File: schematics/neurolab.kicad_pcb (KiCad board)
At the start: 2 copper layers, 127 x 53.6 mm, 167 parts, among them J1 GS3, J10 GS3, J12 GS3, J13 GS3, J14 GS3, J15 GS3, J16 Channel, J17 External, J18 USB_OTG, J19 GS3, J2 GS3, J20 GS2, J21 GS2, J22 GS2, J23 GS2, J24 GS2, J25 GS2, J26 ICSP Port, J27 GS2, J28 GS2, J3 GS3, J32 Bluetooth, J33 Reset Select, J34 GS2, J4 GS2, J5 GS2, J6 GS3, J7 GS3, J8 PowerOut, J9 GS3, Q1 2N7002, U1 ADP1720ARMZ-5, U10 OPA2111KP, U11 AD8422ARMZ, U12 OP4117, U13 OPA2111KP, U14 AD8422ARMZ, U15 OP4117, U16 AD7173, U17 ADR445BR, U18 Arduino, U2 ADP1720ARMZ-3.3, U3 AD8475, U4 AD8475, U5 MAX7480ESA+, U6 MAX7480ESA+, U7 MAX7480ESA+, U8 MAX7480ESA+, U9 TLC555CD, Y1 FA-20H

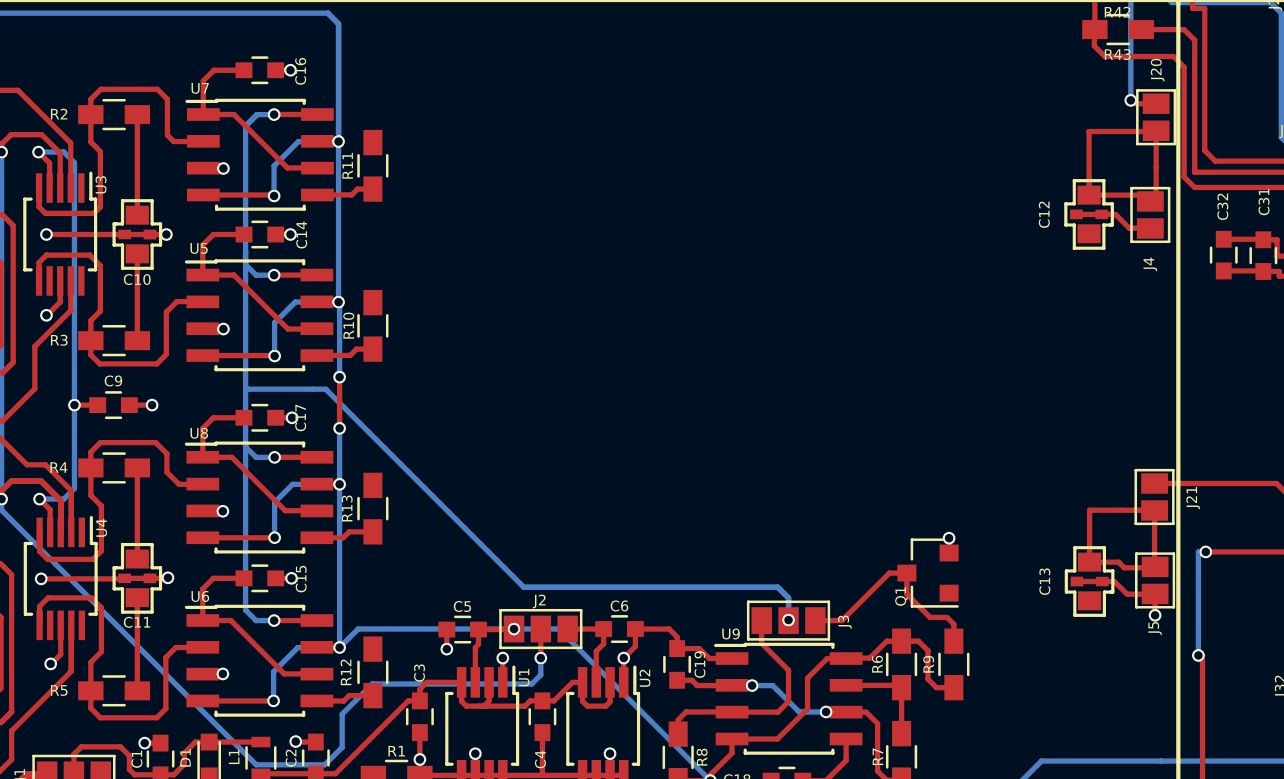
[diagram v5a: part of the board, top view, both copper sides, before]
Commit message: optimize: route parts
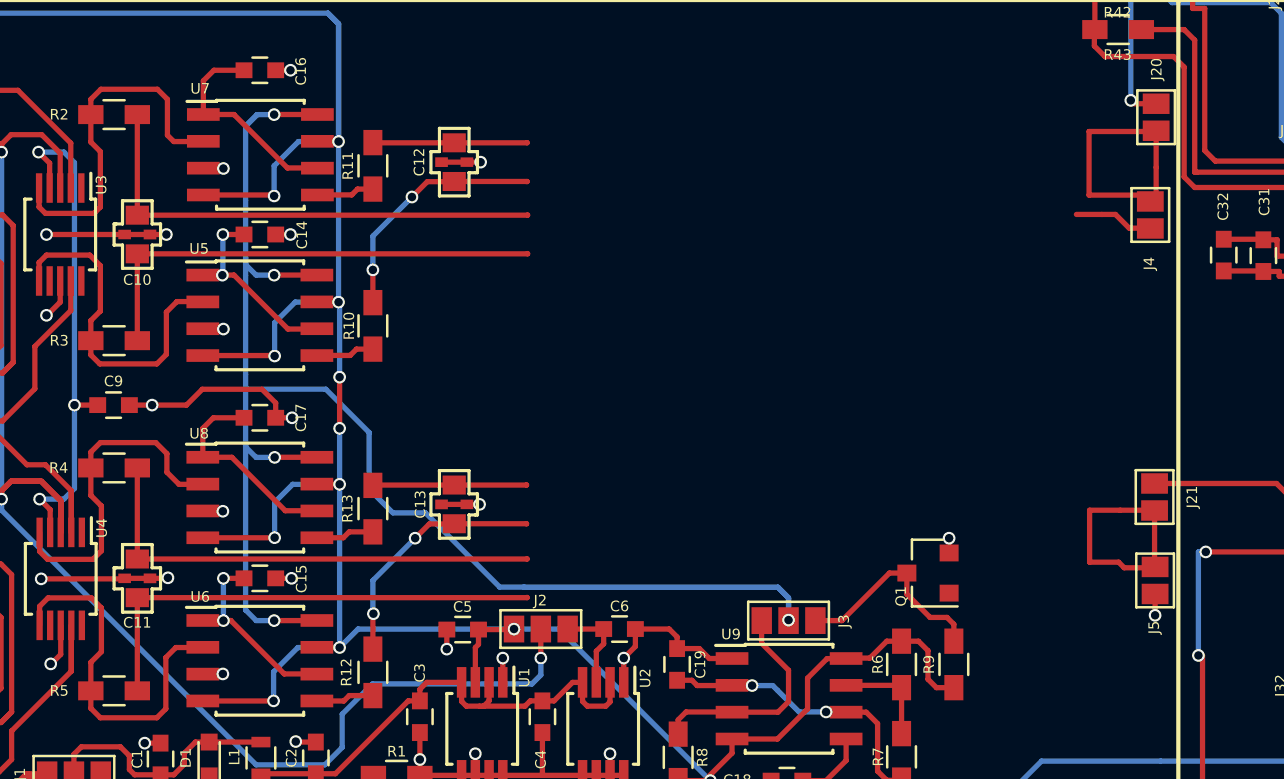
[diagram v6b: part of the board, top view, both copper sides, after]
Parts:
- moved C13 30.3 mm to (157.3, 101.8)
- moved C12 30.2 mm to (157.3, 85.5)
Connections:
- U16 pad 27: /RC Filter 1/+OUTA' -> /ADConverter/AIN4
- U16 pad 28: /RC Filter 1/-OUTA' -> /RC Filter 1/+OUTA'
- U16 pad 29: /ADConverter/AIN4 -> /RC Filter 1/-OUTA'
- U16 pad 32: /RC Filter 1/+OUTB' -> /ADConverter/AIN6
- U16 pad 33: /RC Filter 1/-OUTB' -> /RC Filter 1/+OUTB'
- U16 pad 34: /ADConverter/AIN6 -> /RC Filter 1/-OUTB'
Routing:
- net /RC Filter 1/-OUTA': track 4.11 -> 22.6 mm
- net /RC Filter 1/+OUTA': track 4.76 -> 23.2 mm
- net /RC Filter 1/-OUTB': track 4.41 -> 22.9 mm
- net /RC Filter 1/+OUTB': track 4.31 -> 22.8 mm
- net /ADConverter/AIN6: track 0.16 -> 11.7 mm, vias 0 -> 2
- net /ADConverter/AIN4: track 0.04 -> 11.5 mm, vias 0 -> 2
- net /ADConverter/AIN5: track 13.0 -> 20.4 mm
- net /ADConverter/AIN7: track 11.5 -> 18.8 mm
- net GND: track 238.6 -> 243.6 mm, vias 53 -> 54
- net Net-(C12-Pad2): track 3.78 -> 5.63 mm, vias 0 -> 1
- net /Clock Block/CLK: track 83.7 -> 85.2 mm
- net Net-(C15-Pad1): track 10.1 -> 9.45 mm, vias 0 -> 2
- net Net-(C14-Pad1): track 10.1 -> 9.44 mm, vias 0 -> 2

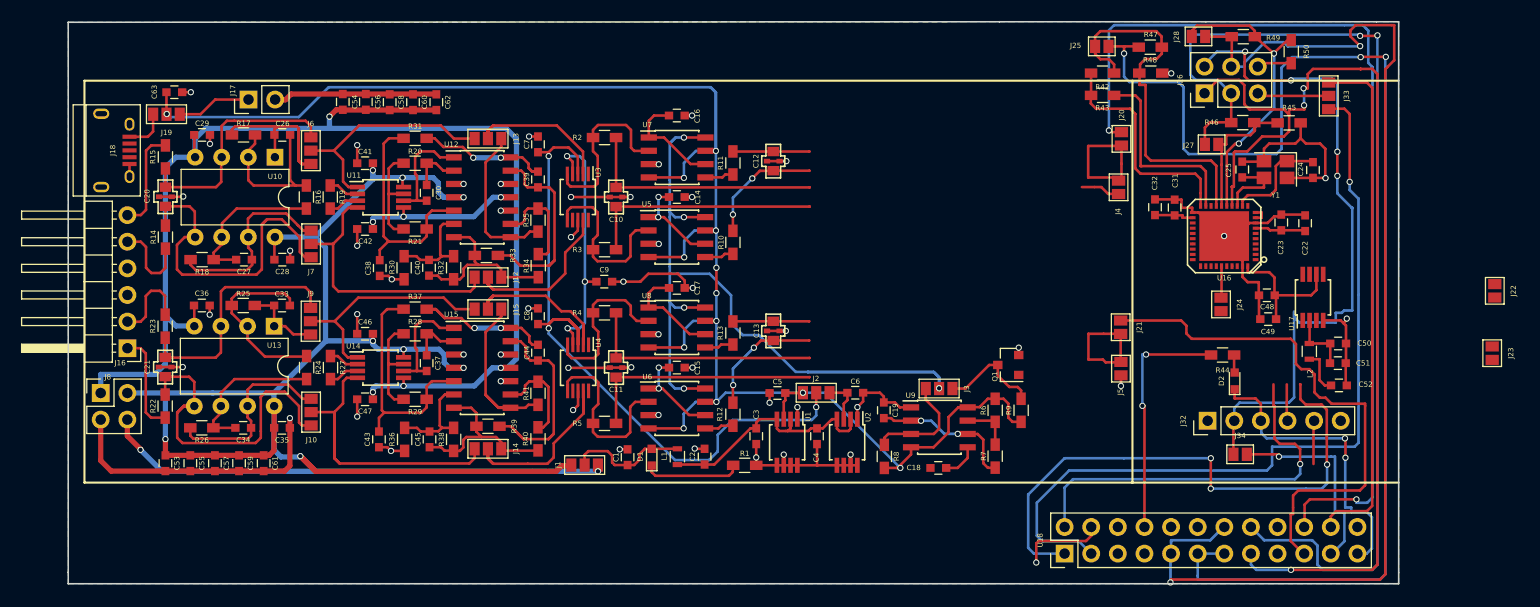
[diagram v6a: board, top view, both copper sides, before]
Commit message: optimize: removed redundant SPI connector
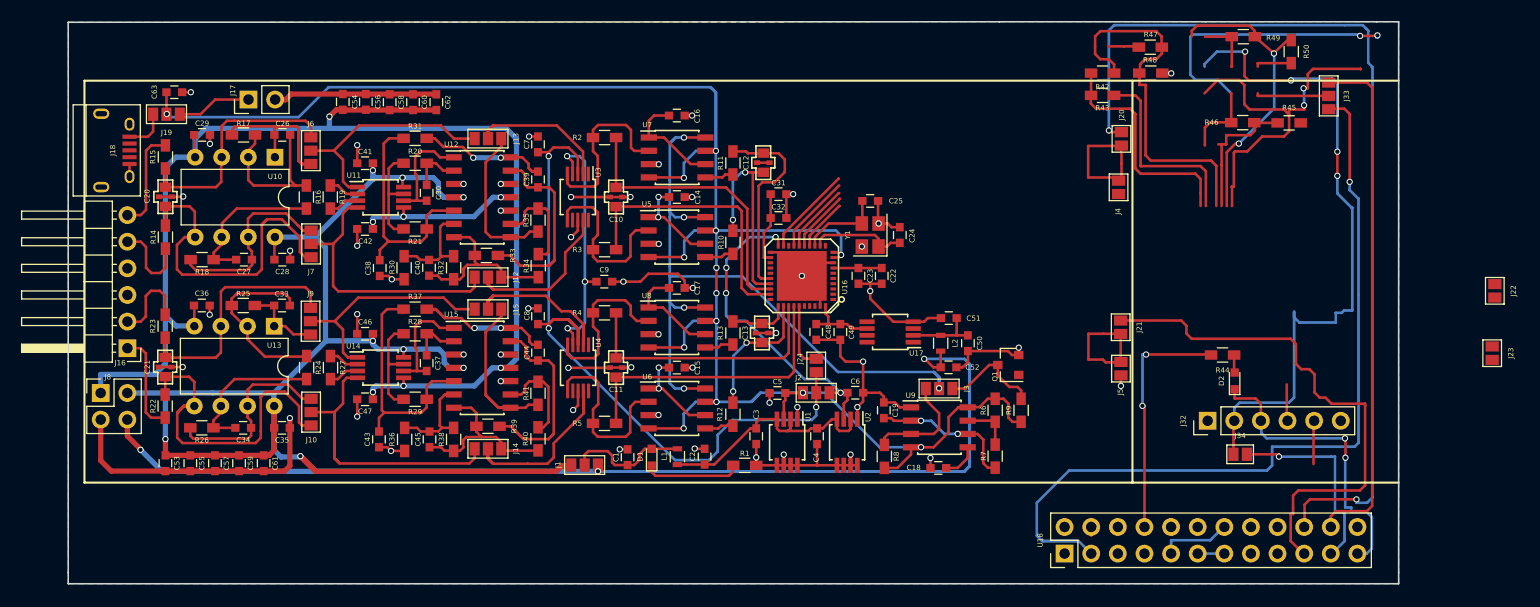
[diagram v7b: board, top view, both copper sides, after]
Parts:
- removed J25, J27, J28: GS2, Connectors:GS2
- removed J26: ICSP Port, Pin_Headers:Pin_Header_Straight_2x03_Pitch2.54mm
- moved C48 43.1 mm to (161.4, 101.8), turned to 270 degrees
- moved C49 40.8 mm to (163.7, 101.8), turned to 270 degrees
- moved C22 40.7 mm to (167.7, 96.5), turned to 270 degrees
- moved C23 40.7 mm to (165.4, 96.5), turned to 270 degrees
- moved U17 40.5 mm to (168.5, 101.8), turned to 180 degrees
- moved U16 40.5 mm to (160.1, 96.5)
- moved C24 39.9 mm to (169.4, 92.6), turned to 90 degrees
- moved Y1 39.2 mm to (166.6, 92.6), turned to 90 degrees
- moved J24 39.1 mm to (161.4, 105.0)
- moved C31 37.8 mm to (157.8, 88.7), turned to 0 degrees
- moved C51 37.4 mm to (174.1, 100.5), turned to 180 degrees
- moved C52 37.3 mm to (174.1, 105.2)
- moved C32 35.9 mm to (157.8, 91.0), turned to 0 degrees
- moved C25 35.6 mm to (166.6, 89.3), turned to 0 degrees
- moved C50 35.3 mm to (175.9, 102.9), turned to 270 degrees
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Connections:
- J33 pad 2: /SPI Connector/RST -> (no net)
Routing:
- net CS: track 118.3 -> 5.50 mm, vias 3 -> 0
- net MISO: track 108.9 -> 12.4 mm, vias 2 -> 0
- net +5.5V: track 53.4 -> 148.7 mm, vias 2 -> 3
- net MOSI: track 97.3 -> 5.02 mm, vias 3 -> 0
- net SCL: track 99.5 -> 7.27 mm, vias 2 -> 0
- net (no net): track 0.00 -> 74.9 mm, vias 0 -> 4
- net TxO: track 56.8 -> 3.55 mm, vias 3 -> 0
- net RxI: track 41.5 -> 4.19 mm, vias 1 -> 0
- net +3V: track 26.4 -> 52.2 mm, vias 0 -> 4
- net +5V: track 175.7 -> 192.9 mm, vias 13 -> 14
- net GND: track 243.6 -> 229.4 mm, vias 54 -> 57
- net /ADConverter/AIN5: track 20.4 -> 32.6 mm
- net /Clock Block/CLK: track 85.2 -> 73.1 mm
- net /ADConverter/AIN4: track 11.5 -> 20.4 mm
- net Net-(R43-Pad1): track 18.7 -> 27.3 mm
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
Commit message: optimize: routing SPI
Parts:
- removed J20, J21, J22, J23: GS2, Connectors:GS2
- moved R50 38.5 mm to (169.6, 85.2), turned to 0 degrees
- moved R45 37.0 mm to (169.6, 79.4)
- moved R49 35.2 mm to (169.6, 87.1), turned to 180 degrees
- moved R43 34.1 mm to (154.7, 82.2)
- moved R42 34.1 mm to (154.7, 79.8)
- moved R48 34.1 mm to (159.7, 82.2)
- moved R47 34.0 mm to (159.7, 79.8), turned to 180 degrees
- moved R46 32.5 mm to (169.6, 81.3), turned to 180 degrees
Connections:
- C10 pad 3: /RC Filter 1/+OUTA' -> AD1
- C11 pad 3: /RC Filter 1/+OUTB' -> AD0
- C12 pad 1: /ADConverter/AIN5 -> AD3
- C13 pad 1: /ADConverter/AIN7 -> AD2
- J4 pad 2: /ADConverter/AIN5 -> AD3
- J5 pad 2: /ADConverter/AIN7 -> AD2
- R11 pad 2: /ADConverter/AIN5 -> AD3
- R13 pad 2: /ADConverter/AIN7 -> AD2
- R2 pad 1: /RC Filter 1/+OUTA' -> AD1
- R4 pad 1: /RC Filter 1/+OUTB' -> AD0
- U16 pad 26: /ADConverter/AIN5 -> AD3
- U16 pad 28: /RC Filter 1/+OUTA' -> AD1
- U16 pad 31: /ADConverter/AIN7 -> AD2
- U16 pad 33: /RC Filter 1/+OUTB' -> AD0
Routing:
- net (no net): track 74.9 -> 3.56 mm, vias 4 -> 1
- net VCC: track 64.9 -> 3.28 mm, vias 4 -> 0
- net /ADConverter/AIN5: track 32.6 -> 0.00 mm
- net +3V: track 52.2 -> 81.7 mm, vias 4 -> 7
- net /ADConverter/DI: track 35.3 -> 5.90 mm, vias 2 -> 0
- net AD1: track 0.00 -> 27.7 mm
- net /RC Filter 1/+OUTA': track 27.7 -> 0.00 mm
- net AD0: track 0.00 -> 25.5 mm
- net /RC Filter 1/+OUTB': track 25.5 -> 0.00 mm
- net /ADConverter/CS: track 43.6 -> 19.3 mm
- net AD3: track 90.2 -> 110.3 mm
- net /ADConverter/AIN7: track 17.3 -> 0.00 mm
- net Net-(R43-Pad1): track 27.3 -> 14.6 mm
- net /ADConverter/SCL: track 15.1 -> 6.64 mm
- net SCL: track 7.27 -> 0.00 mm
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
